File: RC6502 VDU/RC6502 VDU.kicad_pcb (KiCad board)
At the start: 2 copper layers, 99.1 x 99.7 mm, 0 parts

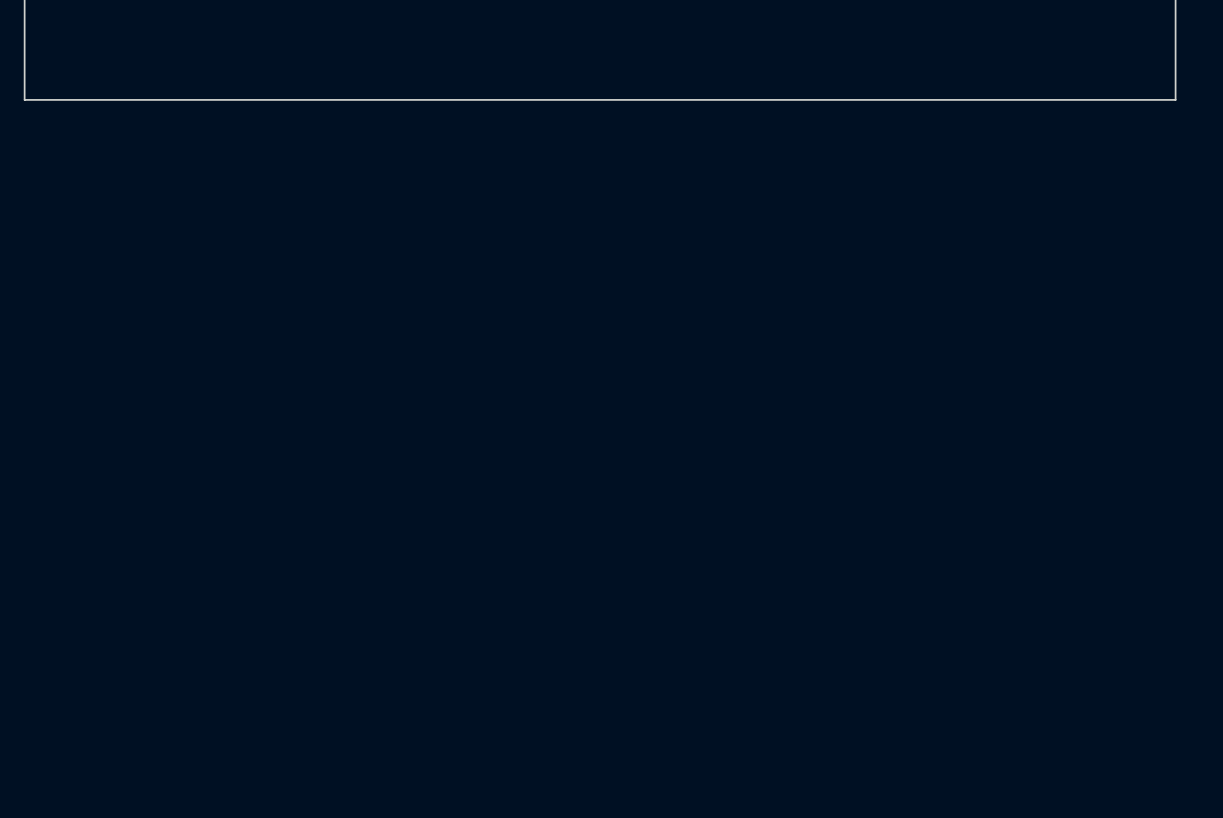
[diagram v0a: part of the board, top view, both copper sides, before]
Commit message: Forced KiCad to actually use GND as ground name
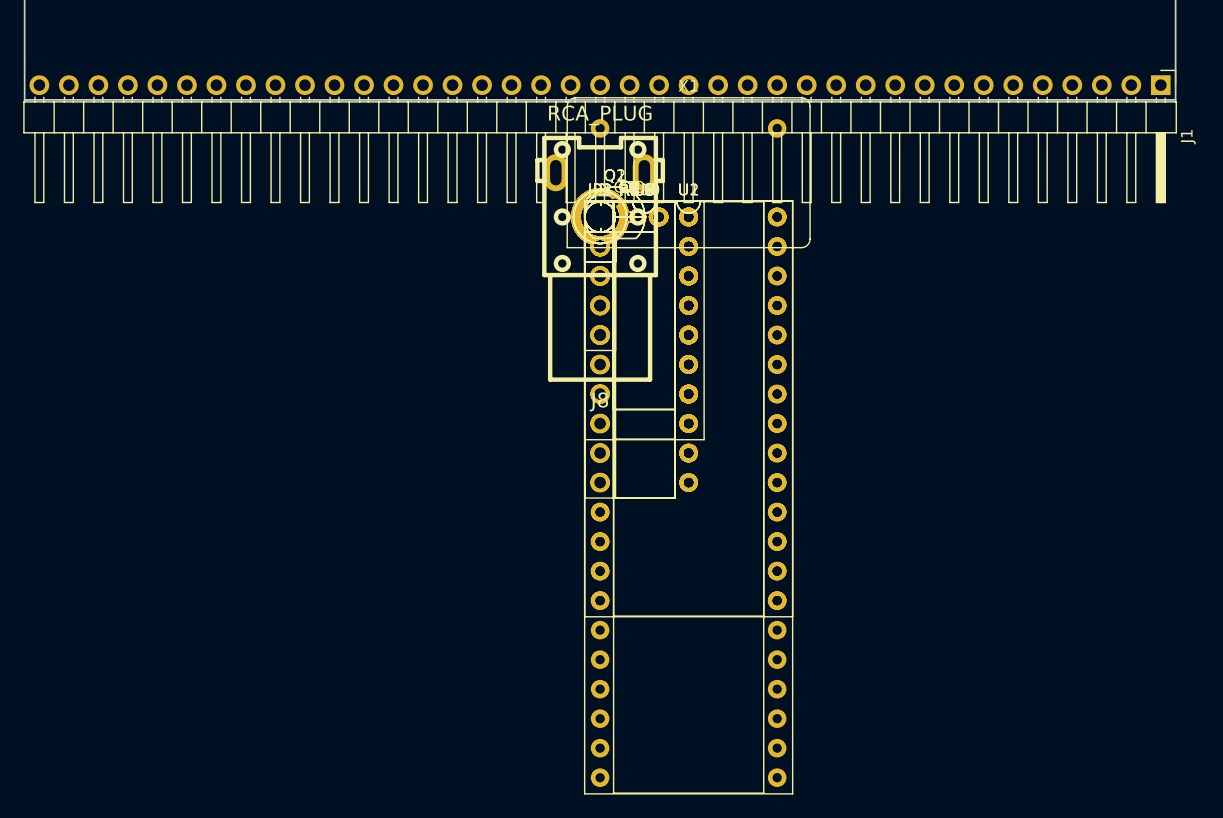
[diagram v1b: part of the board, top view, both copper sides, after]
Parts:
- added C1, C10, C2, C3, C4, C5, C6, C7, C8, C9: 100nF, Capacitors_THT:C_Disc_D4.7mm_W2.5mm_P5.00mm, F.Cu at (102.2, 154.2)
- added J1: RC6502_Backplane, Pin_Headers:Pin_Header_Angled_1x39_Pitch2.54mm, F.Cu at (150.5, 142.9)
- added J2: VDU_BASE, Pin_Headers:Pin_Header_Straight_1x10_Pitch2.54mm, F.Cu at (102.2, 154.2)
- added J3: VIDEO, Pin_Headers:Pin_Header_Straight_1x05_Pitch2.54mm, F.Cu at (102.2, 154.2)
- added J4, J5, J6, J7: Hole, mounting:Mounting, F.Cu at (102.2, 154.2)
- added J8: RCA_PLUG, rca:rca_yellow, F.Cu at (102.2, 154.2)
- added JP1: VDU_EN, Pin_Headers:Pin_Header_Straight_1x02_Pitch2.54mm, F.Cu at (102.2, 154.2)
- added JP2: PHI0_OUT, Pin_Headers:Pin_Header_Straight_1x02_Pitch2.54mm, F.Cu at (102.2, 154.2)
- added JP3: INT_ON_FS, Pin_Headers:Pin_Header_Straight_1x02_Pitch2.54mm, F.Cu at (102.2, 154.2)
- added Q1, Q2: PN2222A, TO_SOT_Packages_THT:TO-92_Molded_Narrow, F.Cu at (102.2, 154.2)
- added R1, R2, R5: 1k, Resistors_THT:R_Axial_DIN0207_L6.3mm_D2.5mm_P5.08mm_Vertical, F.Cu at (102.2, 154.2)
- added R3: 180, Resistors_THT:R_Axial_DIN0207_L6.3mm_D2.5mm_P5.08mm_Vertical, F.Cu at (102.2, 154.2)
- added R4: 6.2k, Resistors_THT:R_Axial_DIN0207_L6.3mm_D2.5mm_P5.08mm_Vertical, F.Cu at (102.2, 154.2)
- added U1: MC6847, Housings_DIP:DIP-40_W15.24mm_Socket, F.Cu at (102.2, 154.2)
- added U10, U9: 74HCT00, Housings_DIP:DIP-14_W7.62mm, F.Cu at (102.2, 154.2)
- added U2: HM62256BLP-7, Housings_DIP:DIP-28_W15.24mm_Socket, F.Cu at (102.2, 154.2)
- added U3, U4: 74LS244, Housings_DIP:DIP-20_W7.62mm, F.Cu at (102.2, 154.2)
- added U5: 74LS245, Housings_DIP:DIP-20_W7.62mm, F.Cu at (102.2, 154.2)
- added U6: 74LS374, Housings_DIP:DIP-20_W7.62mm, F.Cu at (102.2, 154.2)
- added U7: 74HCT138, Housings_DIP:DIP-16_W7.62mm_Socket, F.Cu at (102.2, 154.2)
- added U8: 74HCT04, Housings_DIP:DIP-14_W7.62mm, F.Cu at (102.2, 154.2)
- added X1: 3.579545 MHz, Oscillators:Oscillator_DIP-14, F.Cu at (102.2, 154.2)

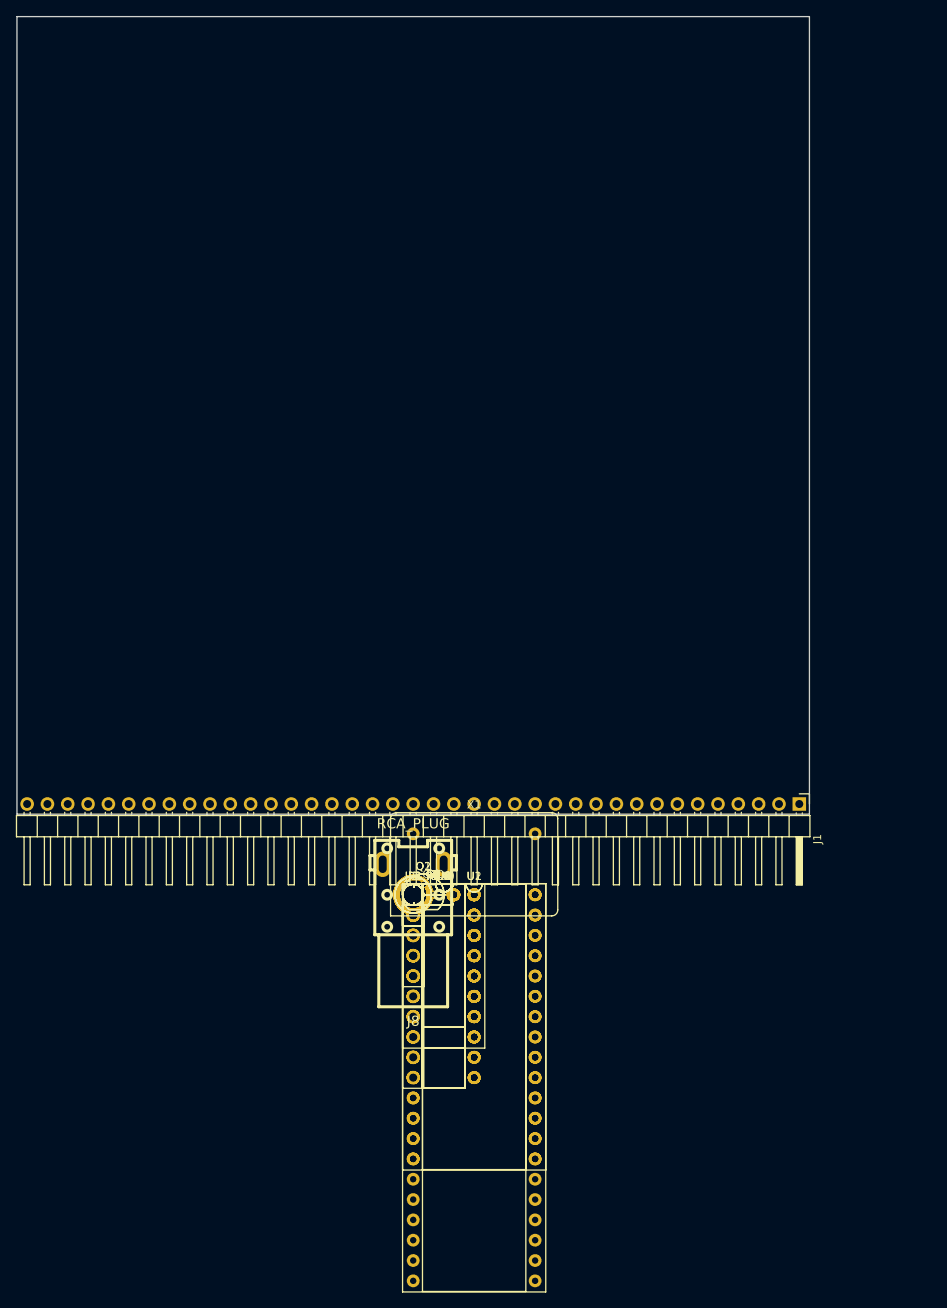
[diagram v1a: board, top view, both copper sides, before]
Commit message: Changed VDU CS logic ins schematic
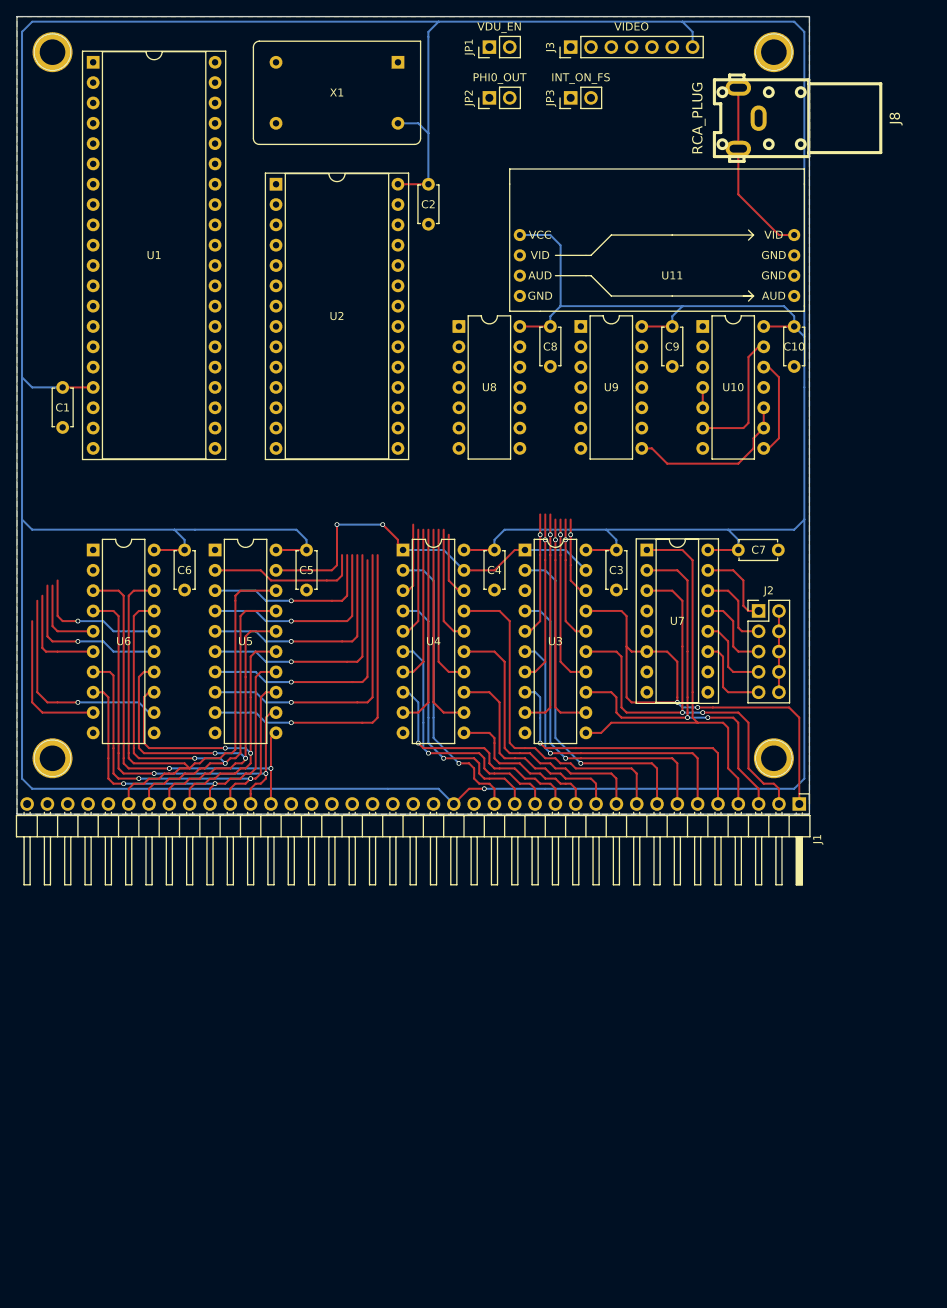
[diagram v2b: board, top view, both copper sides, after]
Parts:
- removed Q1, Q2: PN2222A, TO_SOT_Packages_THT:TO-92_Molded_Narrow
- removed R1, R2, R5: 1k, Resistors_THT:R_Axial_DIN0207_L6.3mm_D2.5mm_P5.08mm_Vertical
- removed R3: 180, Resistors_THT:R_Axial_DIN0207_L6.3mm_D2.5mm_P5.08mm_Vertical
- removed R4: 6.2k, Resistors_THT:R_Axial_DIN0207_L6.3mm_D2.5mm_P5.08mm_Vertical
- added U11: VDU_Port, vdu_amplifier:Amplifier, F.Cu at (134.6, 75.6)
- J2: footprint Pin_Headers:Pin_Header_Straight_1x10_Pitch2.54mm -> Pin_Headers:Pin_Header_Straight_2x05_Pitch2.54mm
- J3: footprint Pin_Headers:Pin_Header_Straight_1x05_Pitch2.54mm -> Pin_Headers:Pin_Header_Straight_1x07_Pitch2.54mm
- moved J4 114.6 mm to (57.1, 48.9)
- moved J7 114.6 mm to (147.3, 48.9)
- moved U1 111.5 mm to (62.2, 50.2)
- moved J3 107.8 mm to (121.9, 48.3), turned to 90 degrees
- moved J8 106.8 mm to (146.7, 57.1), turned to 90 degrees
- moved JP1 106.4 mm to (111.8, 48.3), turned to 90 degrees
- moved X1 104.1 mm to (100.3, 50.2), turned to 180 degrees
- moved JP3 101.5 mm to (121.9, 54.6), turned to 90 degrees
- moved JP2 100.1 mm to (111.8, 54.6), turned to 90 degrees
- moved U2 90.5 mm to (85.1, 65.4)
- moved C2 88.8 mm to (104.1, 65.4), turned to 270 degrees
- moved C10 85.5 mm to (149.9, 83.2), turned to 270 degrees
- moved U10 79.7 mm to (138.4, 83.2)
- moved C9 78.1 mm to (134.6, 83.2), turned to 270 degrees
- moved C1 77.1 mm to (58.4, 90.8), turned to 270 degrees
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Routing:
- net VCC: track 0.00 -> 598.8 mm, vias 0 -> 1
- net D7: track 0.00 -> 73.7 mm
- net ~CS_RAM_EXT: track 0.00 -> 70.1 mm, vias 0 -> 2
- net D6: track 0.00 -> 68.9 mm, vias 0 -> 2
- net A15: track 0.00 -> 61.2 mm, vias 0 -> 2
- net A14: track 0.00 -> 59.1 mm, vias 0 -> 2
- net D5: track 0.00 -> 57.3 mm, vias 0 -> 2
- net A13: track 0.00 -> 55.7 mm, vias 0 -> 2
- net A12: track 0.00 -> 55.4 mm
- net D1: track 0.00 -> 54.7 mm, vias 0 -> 2
- net D0: track 0.00 -> 52.9 mm, vias 0 -> 2
- net D2: track 0.00 -> 50.6 mm, vias 0 -> 2
- net D3: track 0.00 -> 48.8 mm, vias 0 -> 2
- net D4: track 0.00 -> 48.7 mm, vias 0 -> 2
- net A8: track 0.00 -> 42.7 mm, vias 0 -> 1
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- added copper zone on B.Cu, net GND

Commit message: VDU PCB layout done
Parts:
- added C12: 100nF, Capacitors_THT:C_Disc_D4.7mm_W2.5mm_P5.00mm, F.Cu at (123.2, 72.4)
- added U12: 74LS374, Housings_DIP:DIP-20_W7.62mm, F.Cu at (127.0, 78.7)
- J2: footprint Pin_Headers:Pin_Header_Straight_2x05_Pitch2.54mm -> Pin_Headers:Pin_Header_Straight_2x07_Pitch2.54mm
- U10: value 74HCT00 -> 74LS02; footprint Housings_DIP:DIP-14_W7.62mm -> Housings_DIP:DIP-14_W7.62mm_Socket
- U8: value 74HCT04 -> 74LS32; footprint Housings_DIP:DIP-14_W7.62mm -> Housings_DIP:DIP-14_W7.62mm_Socket
- U9: value 74HCT00 -> 74HCT138; footprint Housings_DIP:DIP-14_W7.62mm -> Housings_DIP:DIP-16_W7.62mm_Socket
- X1: footprint Oscillators:Oscillator_DIP-14 -> Oscillator:Oscillator_DIP-14
- moved JP3 86.9 mm to (89.5, 135.3), turned to 0 degrees
- moved JP2 82.2 mm to (95.9, 135.3), turned to 0 degrees
- moved J3 67.3 mm to (58.4, 70.5), turned to 0 degrees
- moved JP1 39.2 mm to (146.1, 67.3)
- moved U8 33.1 mm to (134.6, 102.9), turned to 90 degrees
- moved U11 19.9 mm to (125.7, 57.8)
- moved C10 19.1 mm to (130.8, 83.2)
- moved C8 16.6 mm to (130.8, 95.2)
- moved U10 8.52 mm to (134.6, 90.8), turned to 90 degrees
- moved C9 7.62 mm to (127.0, 83.2)
- moved U9 7.62 mm to (115.6, 83.2)
- moved J2 5.24 mm to (144.1, 113.7)
- moved J8 3.24 mm to (149.9, 57.8)
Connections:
- U10 pad 11: RAM_RW -> GND
- U10 pad 12: Net-(U10-Pad12) -> GND
- U10 pad 13: Net-(U10-Pad13) -> (no net)
- U10 pad 3: ~CS_CTRL_EXT -> Net-(U10-Pad3)
- U10 pad 4: ~VDU_WRITE -> Net-(U10-Pad4)
- U10 pad 5: ~VDU_WRITE -> Net-(U10-Pad5)
- U10 pad 6: Net-(U10-Pad13) -> Net-(U10-Pad6)
- U10 pad 8: Net-(U10-Pad12) -> Net-(U10-Pad1)
- U10 pad 9: ~CS_RAM_EXT -> Net-(U10-Pad4)
- U11 pad 6: (no net) -> GND
- U3 pad 11: A12 -> GND
- U3 pad 12: VA11 -> (no net)
- U3 pad 13: A13 -> GND
- U3 pad 15: A14 -> GND
- U3 pad 17: A15 -> GND
- U3 pad 5: VA14 -> (no net)
- U3 pad 7: VA13 -> (no net)
- U3 pad 8: A11 -> GND
- U3 pad 9: VA12 -> (no net)
- U5 pad 1: RAM_RW -> R/~W
- U6 pad 11: ~CS_CTRL_EXT -> ~REG0
- U7 pad 10: (no net) -> Net-(J2-Pad11)
- U7 pad 9: (no net) -> Net-(J2-Pad13)
- U8 pad 1: VDU_BASE -> GND
- U8 pad 10: Net-(U8-Pad10) -> GND
- U8 pad 11: R/~W -> RAM_RW
- U8 pad 12: Net-(U10-Pad1) -> ~CS_RAM_EXT
- U8 pad 13: ~VDU_CTRL -> R/~W
- U8 pad 2: Net-(U8-Pad2) -> GND
- U8 pad 3: ~VDU_WRITE -> (no net)
- U8 pad 4: Net-(U10-Pad2) -> GND
- U8 pad 5: Net-(U8-Pad5) -> GND
- U8 pad 6: Net-(U8-Pad6) -> (no net)
- U9 pad 10: Net-(U8-Pad2) -> Net-(U10-Pad6)
- U9 pad 11: ~VDU_WRITE -> Net-(U10-Pad5)
- U9 pad 12: PHI2 -> ~REG1
- U9 pad 13: Net-(U8-Pad10) -> ~REG0
- U9 pad 14: VCC -> Net-(U10-Pad3)
- U9 pad 3: Net-(U8-Pad5) -> R/~W
- U9 pad 4: Net-(U8-Pad2) -> GND
- U9 pad 5: Net-(U8-Pad6) -> VDU_BASE
- U9 pad 6: ~VDU_CTRL -> PHI2
- U9 pad 7: GND -> (no net)
- U9 pad 8: ~CS_RAM_EXT -> GND
- U9 pad 9: Net-(U8-Pad5) -> (no net)
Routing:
- net VDU_CLK: track 0.00 -> 167.2 mm, vias 0 -> 5
- net ~VDU_DISABLE: track 0.00 -> 156.8 mm, vias 0 -> 2
- net R/~W: track 0.00 -> 142.7 mm, vias 0 -> 7
- net VD7: track 19.2 -> 151.7 mm, vias 0 -> 5
- net ~FS: track 0.00 -> 130.9 mm, vias 0 -> 2
- net VDU_BASE: track 10.2 -> 138.0 mm, vias 0 -> 2
- net VD6: track 22.4 -> 136.0 mm, vias 1 -> 5
- net VA8: track 10.1 -> 119.7 mm, vias 1 -> 5
- net CSS: track 0.00 -> 108.6 mm, vias 0 -> 2
- net VD0: track 41.4 -> 148.8 mm
- net VA9: track 15.8 -> 118.8 mm, vias 1 -> 6
- net VA7: track 9.15 -> 111.9 mm, vias 0 -> 5
- net VD1: track 38.3 -> 139.9 mm, vias 1 -> 3
- net VD2: track 34.4 -> 131.0 mm, vias 1 -> 3
- net VD5: track 25.6 -> 120.0 mm, vias 1 -> 3
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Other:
- board text added: "$8000"
- board text added: "$9000"
- board text added: "$A000"
- board text added: "$B000"
- board text added: "$C000"
- board text added: "$D000"
- board text added: "$E000"
